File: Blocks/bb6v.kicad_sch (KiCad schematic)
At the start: 17 parts, among them U301 TPS63070RNMR

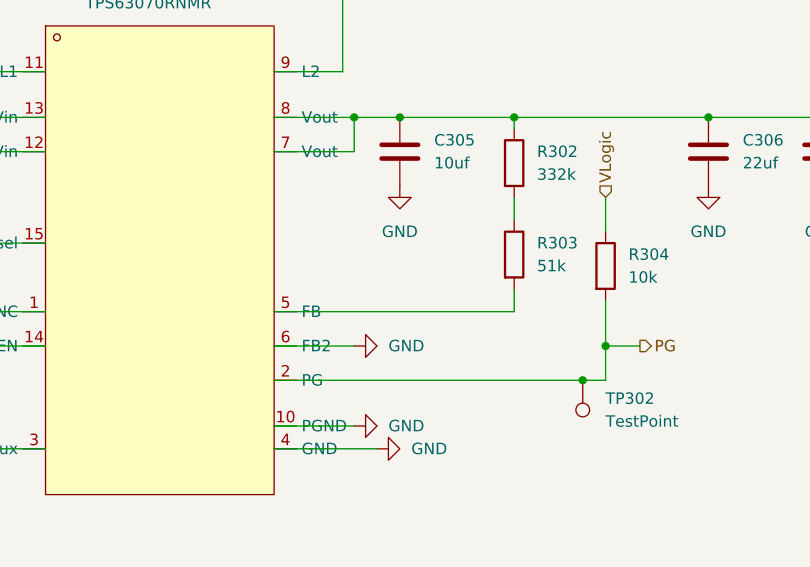
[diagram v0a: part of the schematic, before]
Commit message: fix voltage divider
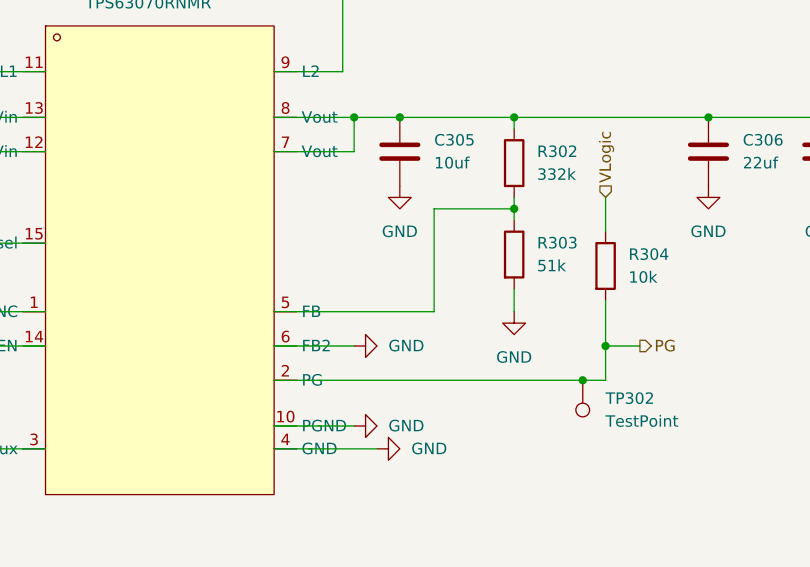
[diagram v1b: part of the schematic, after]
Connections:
- net GND: now also R303.2
- net at R302.2, R303.1: now also U301.5 (FB)
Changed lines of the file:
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@@
 		(color 0 0 0 0)
 	)
+	(junction
+		(at 182.88 100.33)
+		(diameter 0)
+		(color 0 0 0 0)
+	)
 	(wire
 		(pts
@@
 	(wire
 		(pts
-			(xy 156.21 111.76) (xy 182.88 111.76)
-		)
-		(stroke
-			(width 0)
-			(type default)
-		)
-	)
-	(wire
-		(pts
 			(xy 120.65 104.14) (xy 130.81 104.14)
 		)
@@
 	(wire
 		(pts
+			(xy 182.88 100.33) (xy 182.88 99.06)
+		)
+		(stroke
+			(width 0)
+			(type default)
+		)
+	)
+	(wire
+		(pts
+			(xy 173.99 100.33) (xy 173.99 111.76)
+		)
+		(stroke
+			(width 0)
+			(type default)
+		)
+	)
+	(wire
+		(pts
 			(xy 156.21 115.57) (xy 165.1 115.57)
 		)
@@
 	(wire
 		(pts
+			(xy 182.88 100.33) (xy 173.99 100.33)
+		)
+		(stroke
+			(width 0)
+			(type default)
+		)
+	)
+	(wire
+		(pts
 			(xy 156.21 93.98) (xy 165.1 93.98)
 		)
@@
 	(wire
 		(pts
-			(xy 182.88 101.6) (xy 182.88 99.06)
+			(xy 182.88 101.6) (xy 182.88 100.33)
 		)
 		(stroke
@@
 		(pts
 			(xy 101.6 90.17) (xy 109.22 90.17)
+		)
+		(stroke
+			(width 0)
+			(type default)
+		)
+	)
+	(wire
+		(pts
+			(xy 156.21 111.76) (xy 173.99 111.76)
 		)
 		(stroke
@@
 					(unit 1)
 				)
+			)
+		)
+	)
+	(symbol
+		(lib_id "power:GND")
+		(at 182.88 111.76 0)
+		(unit 1)
+		(exclude_from_sim no)
+		(in_bom yes)
+		(on_board yes)
+		(dnp no)
+		(fields_autoplaced yes)
+		(property "Reference" "#PWR01"
+			(at 182.88 118.11 0)
+			(effects
+				(font
+					(size 1.27 1.27)
+				)
+				(hide yes)
+			)
+		)
+		(property "Value" "GND"
+			(at 182.88 116.84 0)
+			(effects
+				(font
+					(size 1.27 1.27)
+				)
+			)
+		)
+		(property "Footprint" ""
+			(at 182.88 111.76 0)
+			(effects
+				(font
+					(size 1.27 1.27)
+				)
+				(hide yes)
+			)
+		)
+		(property "Datasheet" ""
+			(at 182.88 111.76 0)
+			(effects
+				(font
+					(size 1.27 1.27)
+				)
+				(hide yes)
+			)
+		)
+		(property "Description" "Power symbol creates a global label with name \"GND\" , ground"
+			(at 182.88 111.76 0)
+			(effects
+				(font
+					(size 1.27 1.27)
+				)
+				(hide yes)
+			)
+		)
+		(pin "1"
+		)
+		(instances
+			(project ""
+				(path "/48ddfdd8-68fa-4e63-aa18-bc113cdf8cfa/35e7cf5c-95fe-496c-867d-9a2129f85874"
+					(reference "#PWR01")
+					(unit 1)
+				)
